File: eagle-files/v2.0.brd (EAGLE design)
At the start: 24.1 x 78.7 mm, 26 parts, among them U1 MLX90614_

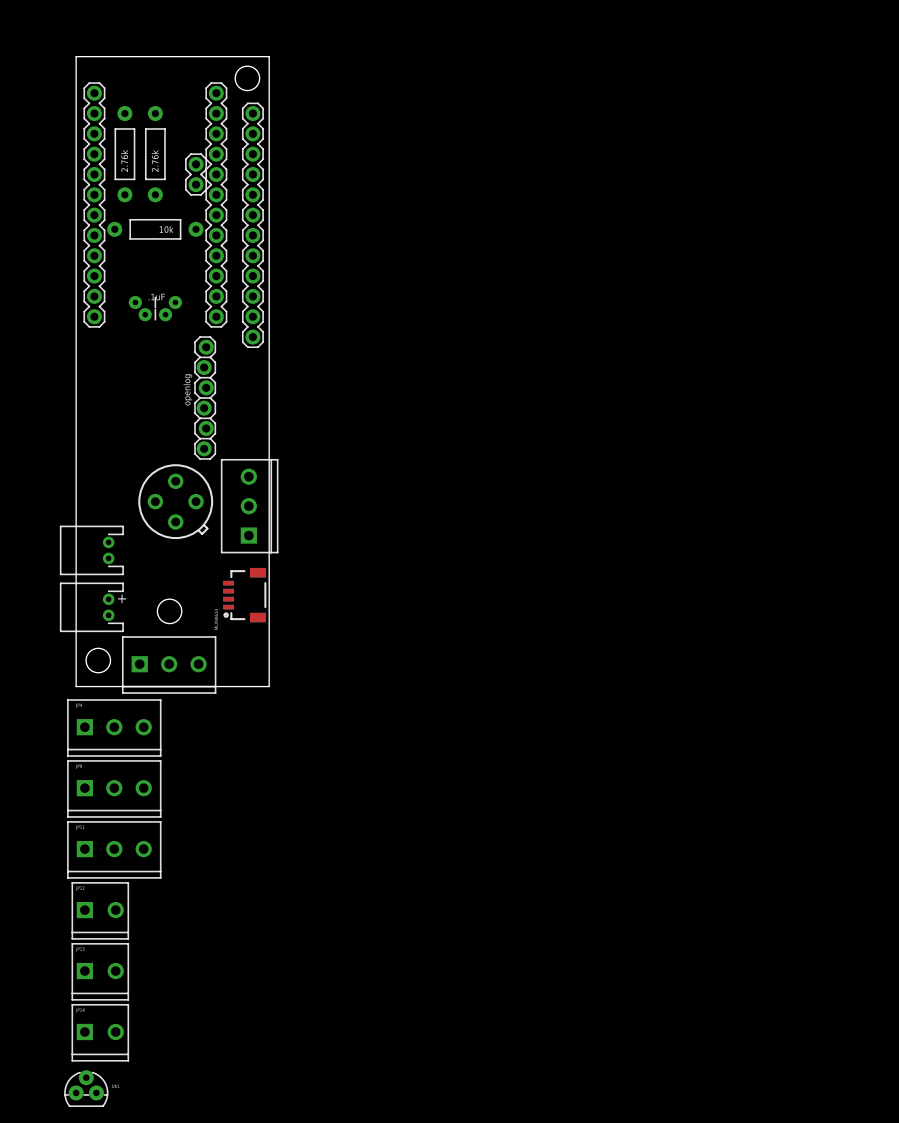
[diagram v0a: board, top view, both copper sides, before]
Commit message: Added all parts to schematic
Added all the bits and pieces needed to the shcematic and did a rough
auto route on the board. This is still assuming that the wheel only
needs 4 pins (power, ground, data1, data2). There is no circuit for
clean reading for the wheel yet. Have not run DRC or ERC.
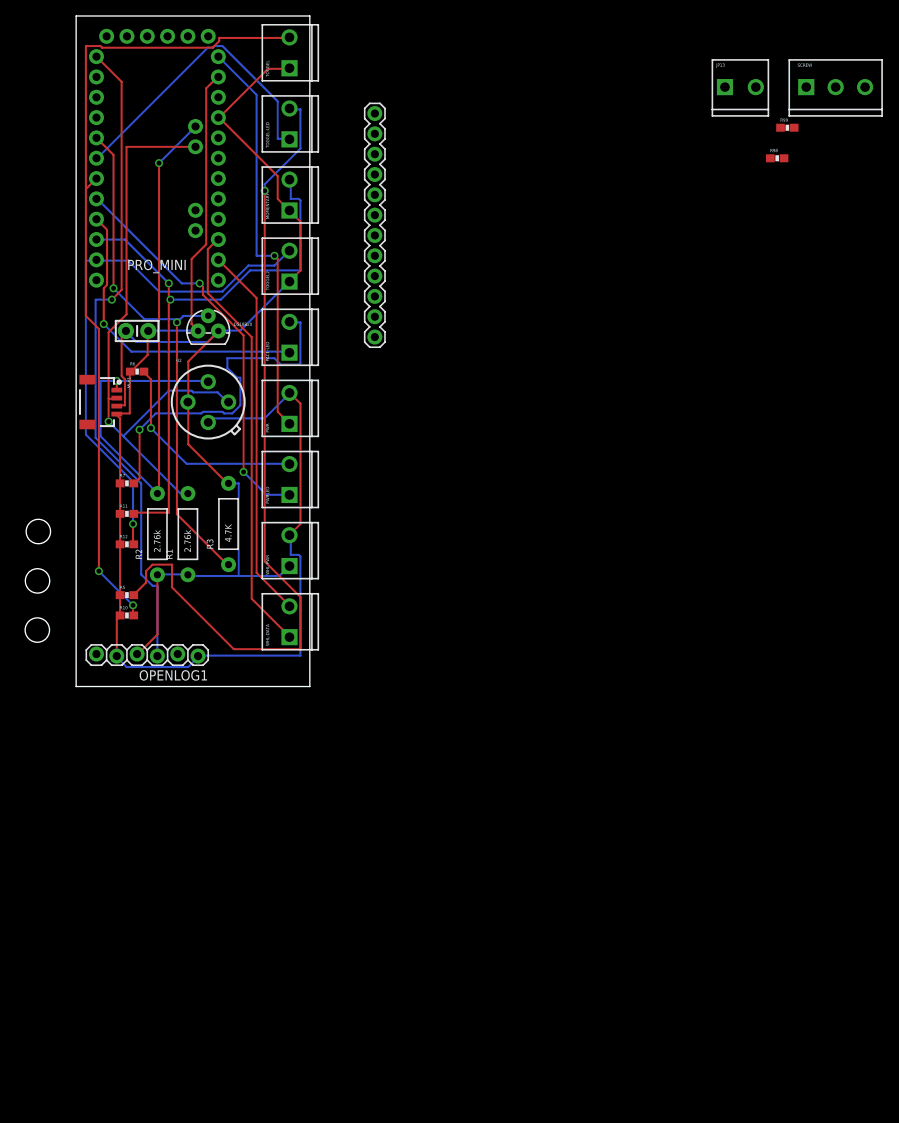
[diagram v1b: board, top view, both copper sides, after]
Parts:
- removed C1: .1uF, SparkFun:CAP-PTH-SMALL
- removed C3: .1u, SparkFun:CAP-PTH-5MM
- removed DISPLAY: DSP, SparkFun:SCREWTERMINAL-3.5MM-3_LOCK.007S
- removed JP1: Power, SparkFun:JST-2-PTH
- removed JP11, JP4, JP9: (no value), SparkFun-Connectors:SCREWTERMINAL-3.5MM-3_LOCK.007S
- removed JP12, JP14: M023.5MM_LOCK, SparkFun-Connectors:SCREWTERMINAL-3.5MM-2_LOCK
- removed JP2: Variable, SparkFun:SCREWTERMINAL-3.5MM-3_LOCK.007S
- removed JP3: Momentary, SparkFun:JST-2-PTH
- removed JP5: A4A5, SparkFun:1X02
- removed MLX90614: (no value), SparkFun-Connectors:1X04-1MM-RA
- removed OPENLOG: OPENLOG, SparkFun:1X06_LOCK
- removed PML: Pro-Dig, SparkFun:1X12
- removed PMR: Pro-Ana, SparkFun:1X12
- removed U$1: TEMPERATURE-SENSOR, SparkFun-Sensors:TO-92
- removed U1: MLX90614_, SparkFun:TO-39
- added C2: .1uF, SparkFun-Capacitors:CAP-PTH-SMALL-KIT
- added DS18B20: (no value), SparkFun-Sensors:TO-92
- added MLX1: (no value), SparkFun-Connectors:1X04-1MM-RA
- added MOMENTARY, PACE-LED, PWR, PWRLED, TOGGEL, TOGGEL-LED, TOGGEL2, WHL-DATA, WHL-PWR: (no value), SparkFun-Connectors:SCREWTERMINAL-3.5MM-2_LOCK
- added OPENLOG1: OPENLOG, SparkFun:1X06_LOCK
- added PRO_MINI: ARDUINO_PRO_MINI, SparkFun-Boards:ARDUINO_PRO_MINI
- added R10, R11, R12, R98: 10K, SparkFun-Resistors:0603-RES
- added R5, R6, R7, R99: 330, SparkFun-Resistors:0603-RES
- added SCREW: (no value), SparkFun-Connectors:SCREWTERMINAL-3.5MM-3_LOCK.007S
- added U2: MLX90614_, SparkFun:TO-39
- R3: value 10k -> 4.7K
- moved JP13 136.4 mm to (81.3, 74.9)
- moved JP7 62.4 mm to (-4.72, 19.4)
- moved R1 47.7 mm to (14.0, 19.1)
- moved R2 47.7 mm to (10.2, 19.1)
- moved R3 37.9 mm to (19.1, 20.3), turned to 90 degrees
- moved JP8 16.9 mm to (-4.83, 13.2)
- moved PMLB 15.2 mm to (37.3, 71.6)
- moved JP6 8.52 mm to (-4.85, 7.06)
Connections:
- removed net N$16: C1.1, C3.1, DISPLAY.3, JP2.1, JP3.1, MLX90614.3, OPENLOG.4, PMLB.5, PMR.4, R1.P$2, R2.P$2, U1.3
- removed net N$20: PML.8
- removed net N$21: PML.7
- removed net N$22: PML.6
- removed net SENSOR: JP5.2, MLX90614.1, R1.P$1, U1.1
- removed net VCC: JP1.2, PMLB.3, PMR.1
- new net 5V: C2.1, DS18B20.3, MLX1.3, MOMENTARY.1, OPENLOG1.4, PRO_MINI.21, R1.P$1, R2.P$1, R3.P$2, TOGGEL.1, TOGGEL2.1, U2.3, WHL-PWR.1
- new net N$1: PRO_MINI.7, R10.2, TOGGEL.2
- new net N$18: PRO_MINI.11, R12.2, TOGGEL2.2
- new net N$7: MLX1.1, PRO_MINI.A5, R2.P$2, U2.2
- net GND: now also C2.2, DS18B20.1, MLX1.4, OPENLOG1.1, OPENLOG1.5, PRO_MINI.23, PWR.2, R10.1, R11.1, R12.1, R5.1, R6.1, R7.1, U2.4, WHL-PWR.2; no longer C1.2, C3.2, DISPLAY.2, JP1.1, JP2.2, MLX90614.4, OPENLOG.1, OPENLOG.5, PML.9, PMLB.4, PMR.2, R3.P$1, U1.4
- net N$10: now also MOMENTARY.2, PRO_MINI.10, R11.2; no longer PMLB.11, PMR.11
- net N$11: now also PRO_MINI.14, WHL-DATA.2; no longer PMLB.10, PMR.10
- net N$12: now also PRO_MINI.6, TOGGEL-LED.1; no longer PMLB.9, PMR.9
- net N$13: now also PACE-LED.1, PRO_MINI.9; no longer PMLB.8, PMR.7
- net N$14: now also PWRLED.2, R6.2; no longer PMLB.7, PMR.6
- net N$15: now also PACE-LED.2, R7.2; no longer PMLB.6, PMR.5
- net N$2: now also DS18B20.2, PRO_MINI.5, R3.P$1; no longer JP5.1, MLX90614.2, R2.P$1, U1.2
- net N$3: now also PRO_MINI.15, WHL-DATA.1; no longer JP3.2, PML.5, R3.P$2
- net N$4: now also PRO_MINI.24, PWR.1; no longer DISPLAY.1, PML.4
- net N$5: now also R5.2, TOGGEL-LED.2; no longer JP2.3, PMR.8
- net N$6: now also PRO_MINI.8, PWRLED.1; no longer OPENLOG.3, PML.12, PMLB.1
- net N$8: now also OPENLOG1.3, PRO_MINI.1; no longer PML.11, PMLB.2
- net N$9: now also MLX1.2, PRO_MINI.A4, R1.P$2, U2.1; no longer PMLB.12, PMR.12
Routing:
- net GND: track 0.00 -> 154.7 mm
- net 5V: track 0.00 -> 135.6 mm
- net N$5: track 0.00 -> 101.9 mm, vias 0 -> 1
- net N$1: track 0.00 -> 101.8 mm, vias 0 -> 2
- net N$8: track 0.00 -> 82.3 mm, vias 0 -> 1
- net N$7: track 0.00 -> 79.5 mm, vias 0 -> 2
- net N$10: track 0.00 -> 74.9 mm, vias 0 -> 2
- net N$9: track 0.00 -> 74.7 mm, vias 0 -> 1
- net N$18: track 0.00 -> 67.2 mm, vias 0 -> 1
- net N$2: track 0.00 -> 66.9 mm, vias 0 -> 2
- net N$3: track 0.00 -> 54.5 mm
- net N$4: track 0.00 -> 50.9 mm, vias 0 -> 1
- net N$6: track 0.00 -> 50.0 mm, vias 0 -> 2
- net N$11: track 0.00 -> 47.0 mm
- net N$15: track 0.00 -> 43.9 mm, vias 0 -> 1
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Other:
- board size 24.1 x 78.7 mm -> 29.2 x 83.8 mm
- board text removed: "+"
- board text removed: ".1uF"
- board text removed: "1"
- board text removed: "2"
- board text removed: "3"
- board text removed: "4"
- board text removed: "6"
- board text removed: "A0"
- board text removed: "GND"
- board text removed: "RAW"
- board text removed: "SENSOR"
- board text removed: "ThermaLocoLogger"
- board text removed: "VCC"
- board text removed: "display"
- board text removed: "momentary"
- board text removed: "openlog"
- board text removed: "variable"

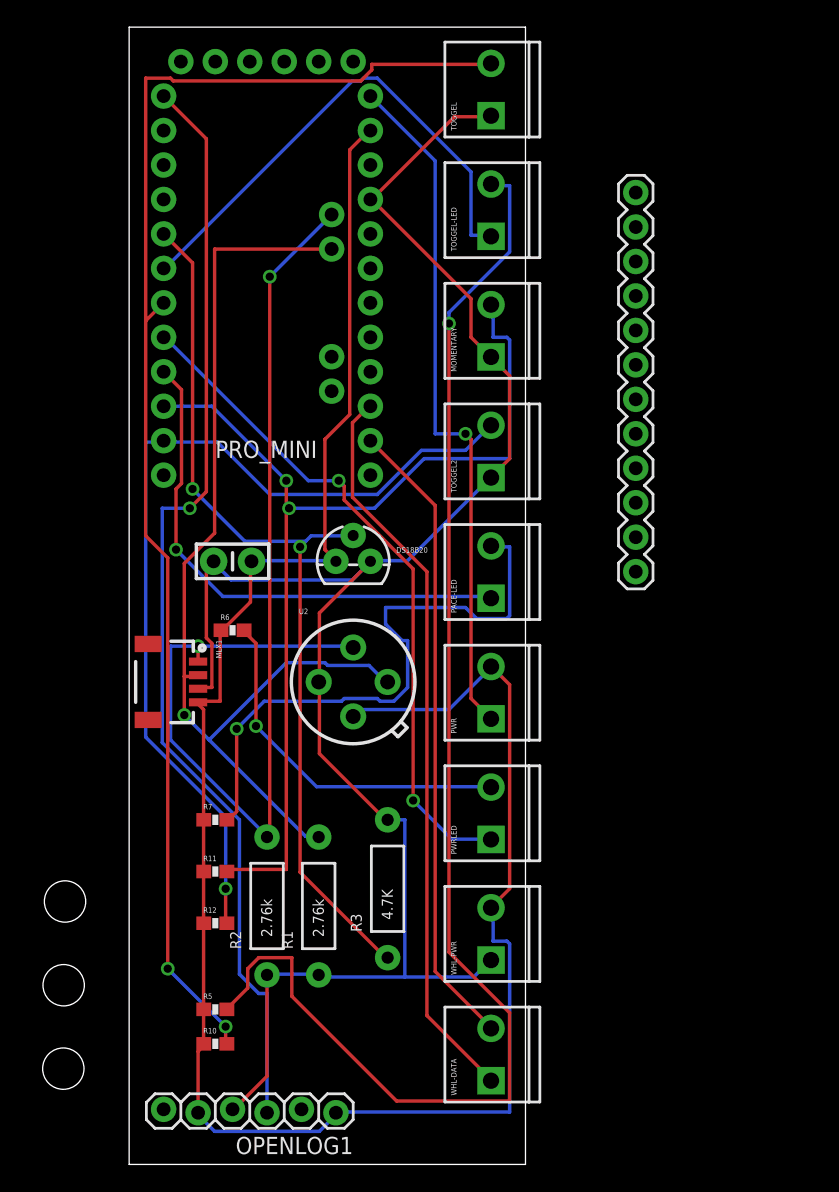
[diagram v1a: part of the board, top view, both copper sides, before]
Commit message: added a few new compnents
Added compnents and the ground plane. Looking at breaking out the reset
button, but the pins are all blocked.
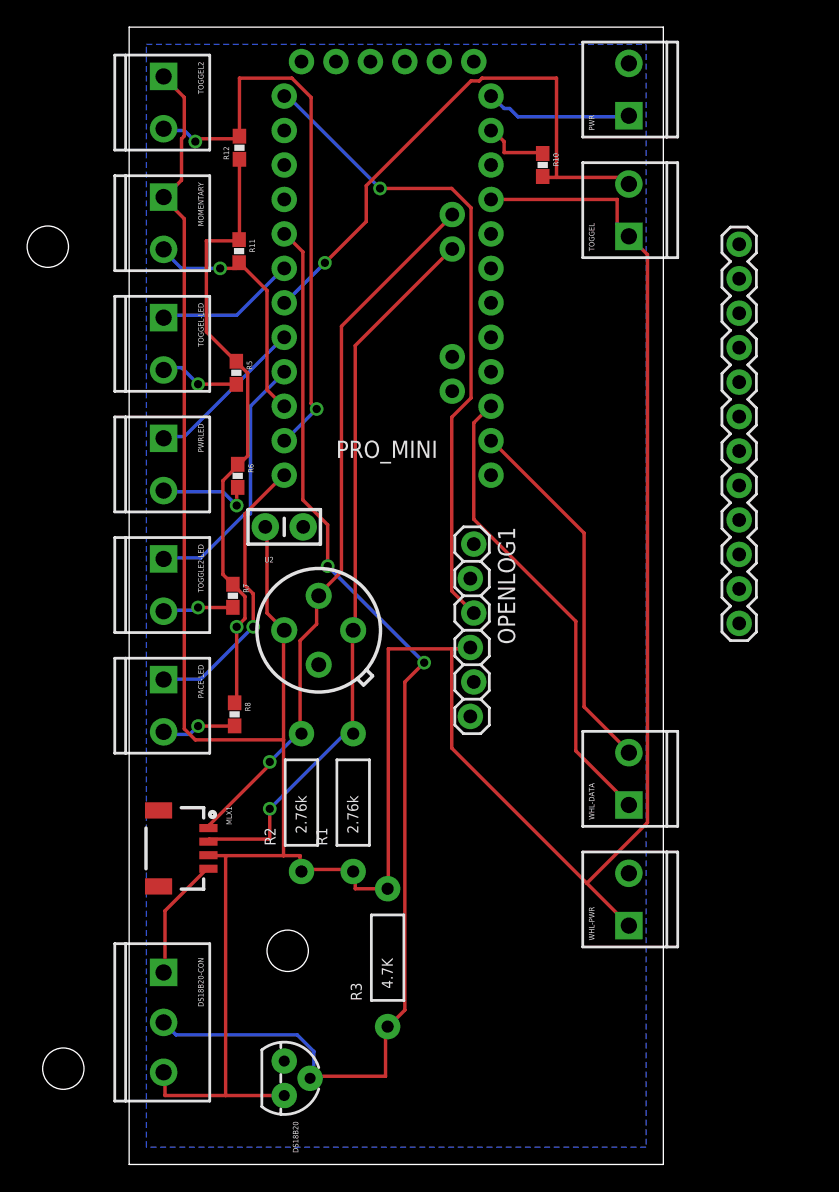
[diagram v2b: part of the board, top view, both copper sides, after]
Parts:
- added DS18B20-CON: CON, SparkFun-Connectors:SCREWTERMINAL-3.5MM-3_LOCK.007S
- added R8: 330, SparkFun-Resistors:0603-RES
- added TOGGLE2-LED: (no value), SparkFun-Connectors:SCREWTERMINAL-3.5MM-2_LOCK
- MLX1: value (none) -> MOLEX
- moved R10 69.1 mm to (30.5, 73.7), turned to 270 degrees
- moved R12 57.2 mm to (8.13, 74.9), turned to 90 degrees
- moved JP7 48.3 mm to (-5.99, 67.6)
- moved R5 46.9 mm to (7.90, 58.3), turned to 270 degrees
- moved R11 45.8 mm to (8.10, 67.3), turned to 270 degrees
- moved PWR 45.6 mm to (36.8, 77.5)
- moved OPENLOG1 43.1 mm to (25.4, 45.7), turned to 270 degrees
- moved DS18B20 38.4 mm to (11.4, 6.35), turned to 270 degrees
- moved TOGGEL2 37.9 mm to (2.54, 80.0), turned to 270 degrees
- moved PWRLED 37.9 mm to (2.54, 53.3), turned to 270 degrees
- moved MOMENTARY 26.7 mm to (2.54, 71.1), turned to 270 degrees
- moved PACE-LED 25.0 mm to (2.54, 35.6), turned to 270 degrees
- moved TOGGEL-LED 25.0 mm to (2.54, 62.2), turned to 270 degrees
- moved WHL-DATA 22.7 mm to (36.8, 26.7)
- moved JP8 16.7 mm to (11.7, 15.7)
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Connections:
- new net N$16: PACE-LED.2, R8.2
- new net N$17: PACE-LED.1, PRO_MINI.12
- net 5V: now also DS18B20-CON.3
- net GND: now also DS18B20-CON.1, R8.1
- net N$13: now also TOGGLE2-LED.1; no longer PACE-LED.1
- net N$15: now also TOGGLE2-LED.2; no longer PACE-LED.2
- net N$2: now also DS18B20-CON.2
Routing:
- net 5V: track 135.6 -> 238.5 mm
- net N$5: track 101.9 -> 5.96 mm
- net GND: track 154.7 -> 59.6 mm, vias 0 -> 1
- net N$1: track 101.8 -> 42.6 mm, vias 2 -> 1
- net N$10: track 74.9 -> 18.6 mm, vias 2 -> 1
- net N$4: track 50.9 -> 10.8 mm, vias 1 -> 0
- net N$15: track 43.9 -> 5.21 mm
- net N$6: track 50.0 -> 12.0 mm, vias 2 -> 0
- net N$8: track 82.3 -> 48.3 mm
- net N$12: track 37.5 -> 10.4 mm
- net N$7: track 79.5 -> 52.9 mm, vias 2 -> 1
- net N$18: track 67.2 -> 43.0 mm, vias 1 -> 2
- net N$17: track 0.00 -> 20.9 mm, vias 0 -> 1
- net N$2: track 66.9 -> 87.5 mm
- net N$9: track 74.7 -> 54.2 mm
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- added copper zone on layer 16, net GND
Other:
- board size 29.2 x 83.8 mm -> 39.4 x 83.8 mm

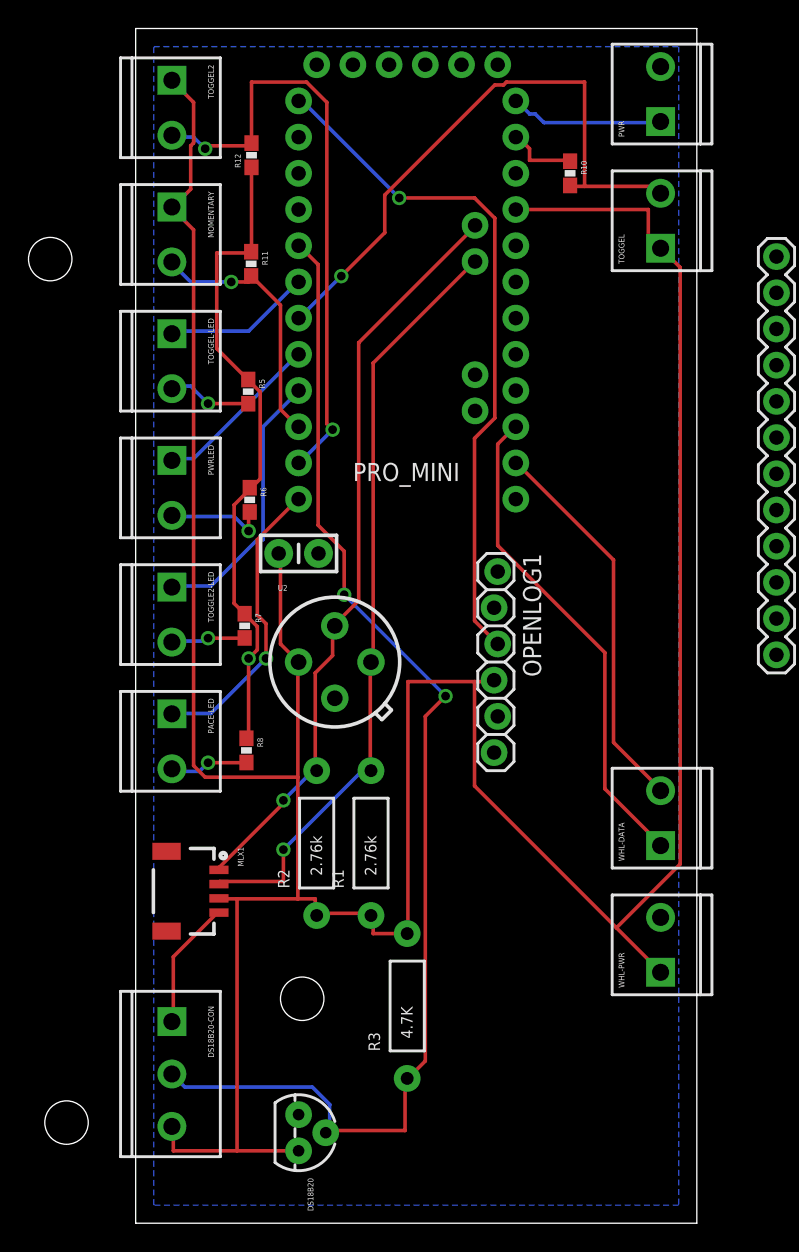
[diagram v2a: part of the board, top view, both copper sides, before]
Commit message: added reset switch and flipped board
Moved parts around to make more room. I added a reset button, but I am
not sure it is wired correctly, I need to test it on an Uno to make
sure that I am not crazy.
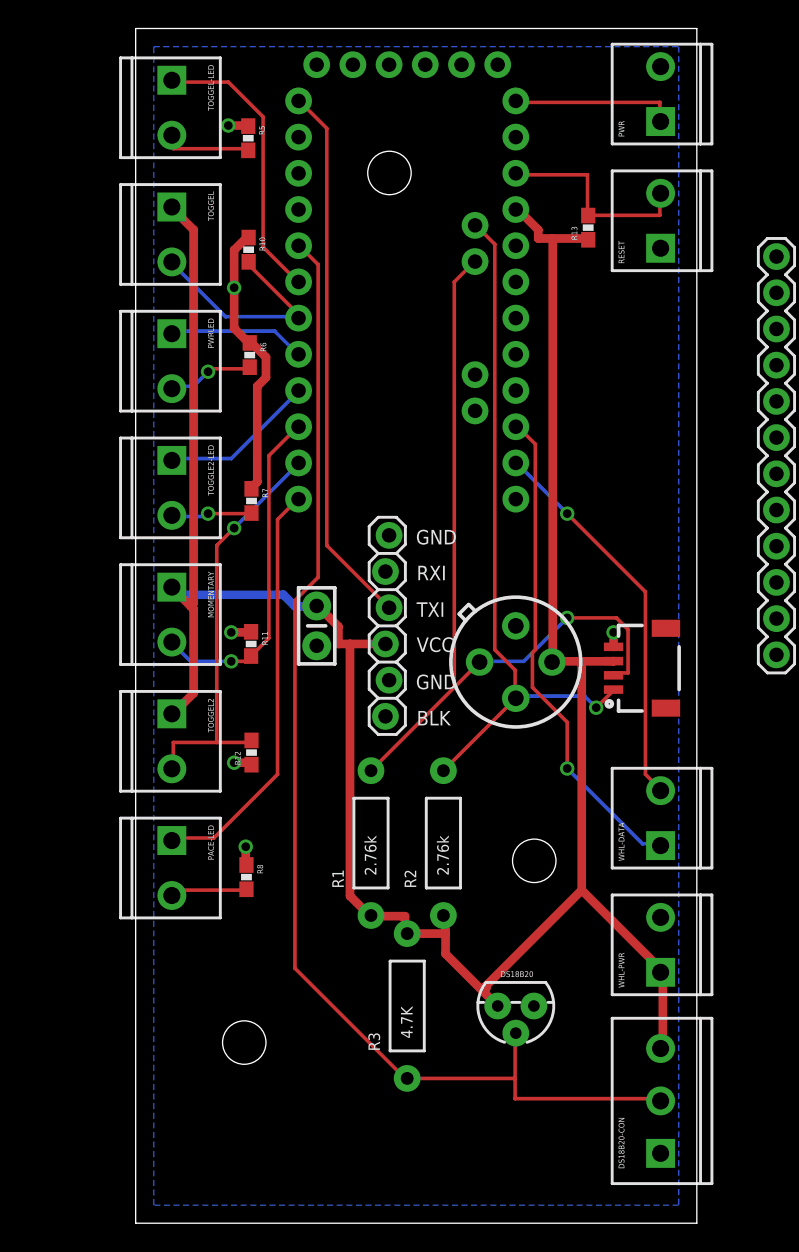
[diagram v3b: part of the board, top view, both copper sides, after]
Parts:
- added R13: 10K, SparkFun-Resistors:0603-RES
- added RESET: (no value), SparkFun-Connectors:SCREWTERMINAL-3.5MM-2_LOCK
- moved TOGGEL2 44.5 mm to (2.54, 35.6)
- moved R12 41.9 mm to (8.13, 33.0)
- moved JP6 37.6 mm to (28.0, 25.4)
- moved DS18B20-CON 35.4 mm to (36.8, 5.08), turned to 90 degrees
- moved TOGGEL 34.4 mm to (2.54, 71.1), turned to 270 degrees
- moved MLX1 31.8 mm to (33.5, 38.9), turned to 90 degrees
- moved MOMENTARY 26.7 mm to (2.54, 44.5)
- moved R11 26.7 mm to (8.10, 40.6)
- moved JP7 24.6 mm to (17.8, 73.7)
- moved R10 23.2 mm to (7.92, 68.3)
- moved TOGGEL-LED 17.8 mm to (2.54, 80.0)
- moved R5 17.8 mm to (7.90, 76.1)
- moved DS18B20 17.6 mm to (26.7, 15.2), turned to 180 degrees
- moved U2 12.7 mm to (26.7, 39.4), turned to 180 degrees
- moved R6 10.2 mm to (8.00, 60.9)
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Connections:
- new net N$19: PRO_MINI.22, R13.2, RESET.2
- net 5V: now also R13.1
- net GND: now also RESET.1
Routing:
- net 5V: track 238.5 -> 170.3 mm
- net GND: track 59.6 -> 26.3 mm, vias 1 -> 6
- net N$1: track 42.6 -> 16.0 mm, vias 1 -> 0
- net N$19: track 0.00 -> 14.5 mm
- net N$18: track 43.0 -> 29.5 mm, vias 2 -> 1
- net N$8: track 48.3 -> 38.2 mm, vias 1 -> 0
- net N$12: track 10.4 -> 20.1 mm
- net N$17: track 20.9 -> 29.3 mm, vias 1 -> 0
- net N$13: track 19.3 -> 10.9 mm
- net N$10: track 18.6 -> 23.9 mm
- net N$7: track 52.9 -> 49.4 mm
- net N$9: track 54.2 -> 57.5 mm
- net N$6: track 12.0 -> 9.67 mm
- net N$2: track 87.5 -> 85.5 mm, vias 2 -> 0
- net N$14: track 7.19 -> 6.25 mm
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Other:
- board text added: "BLK"
- board text added: "GND"
- board text added: "RXI"
- board text added: "TXI"
- board text added: "VCC"

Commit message: Added an analog hookup.
Moved a few things, but not much.
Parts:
- removed PMLB: Side, SparkFun:1X12
- added A0: (no value), SparkFun-Connectors:SCREWTERMINAL-3.5MM-3_LOCK.007S
- moved DS18B20 3.81 mm to (26.7, 11.4)
- moved MLX1 2.54 mm to (33.5, 41.5)
- moved U2 2.54 mm to (26.7, 41.9)
- moved WHL-DATA 1.27 mm to (36.8, 25.4)
- moved DS18B20-CON 1.27 mm to (36.8, 3.81)
- moved WHL-PWR 1.27 mm to (36.8, 16.5)
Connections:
- new net N$20: A0.3, PRO_MINI.17
- net 5V: now also A0.1
- net GND: now also A0.2
- net N$11: now also PRO_MINI.13; no longer PRO_MINI.14
- net N$3: now also PRO_MINI.14; no longer PRO_MINI.15
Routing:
- net 5V: track 170.3 -> 196.2 mm
- net GND: track 26.3 -> 43.0 mm, vias 6 -> 5
- net N$20: track 0.00 -> 11.0 mm
- net N$9: track 57.5 -> 54.9 mm
- net N$2: track 85.5 -> 83.5 mm
- net N$3: track 34.6 -> 33.8 mm
